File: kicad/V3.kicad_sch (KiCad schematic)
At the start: 3 parts, among them U1 SuperMini nRF52840

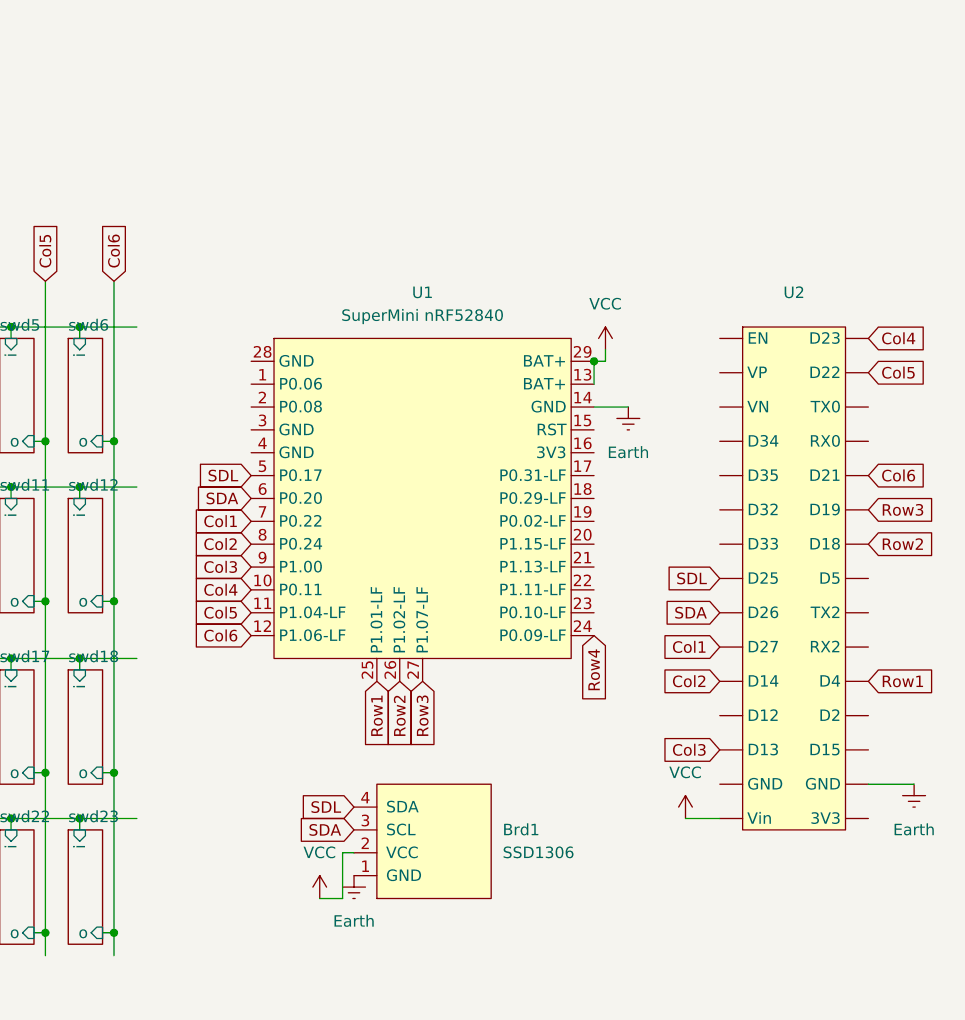
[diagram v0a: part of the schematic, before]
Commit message: change to esp32
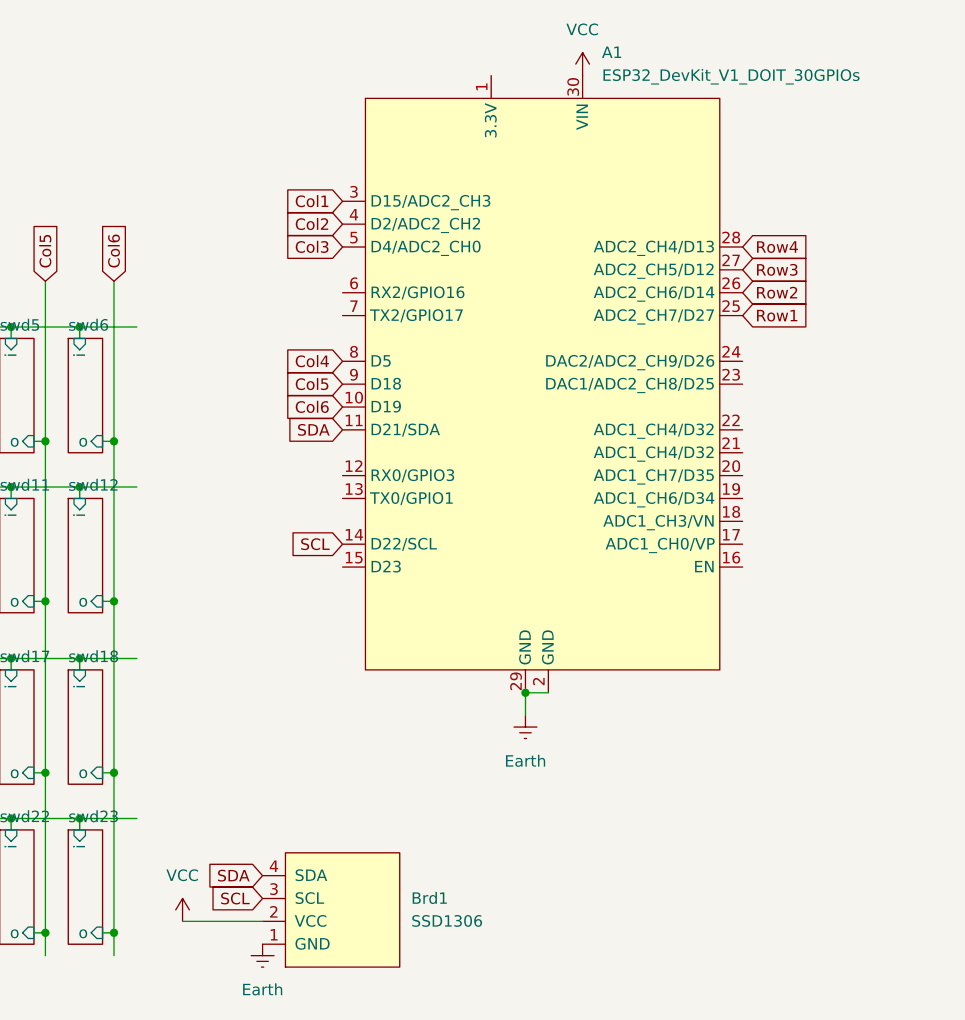
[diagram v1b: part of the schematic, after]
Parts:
- removed U1: SuperMini nRF52840, PCM_marbastlib-xp-promicroish:SuperMini_nRF52840_AH_USBup, symbol PCM_marbastlib-promicroish:SuperMini_nRF52840
- removed U2: ~, symbol Library:Esp32_Dev_Module
- added A1: ESP32_DevKit_V1_DOIT_30GPIOs, PCM_SL_Development_Boards:DOIT_ESP32_DEVKIT_30Pins, symbol PCM_SL_Development_Board:ESP32_DevKit_V1_DOIT_30GPIOs
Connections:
- net SDL is gone; now on net SDA: Brd1.4 (SDA)
- net Col1: now also A1.3 (D15/ADC2_CH3)
- net Col2: now also A1.4 (D2/ADC2_CH2)
- net Col3: now also A1.5 (D4/ADC2_CH0)
- net Col4: now also A1.8 (D5)
- net Col5: now also A1.9 (D18)
- net Col6: now also A1.10 (D19)
- net Earth: now also A1.2 (GND), A1.29 (GND)
- net Row1: now also A1.25 (ADC2_CH7/D27)
- net Row2: now also A1.26 (ADC2_CH6/D14)
- net Row3: now also A1.27 (ADC2_CH5/D12)
- net Row4: now also A1.28 (ADC2_CH4/D13)
- net SDA: now also A1.11 (D21/SDA); no longer Brd1.3 (SCL)
- net VCC: now also A1.30 (VIN)
- new net SCL: A1.14 (D22/SCL), Brd1.3 (SCL)
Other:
- moved on the sheet: Brd1

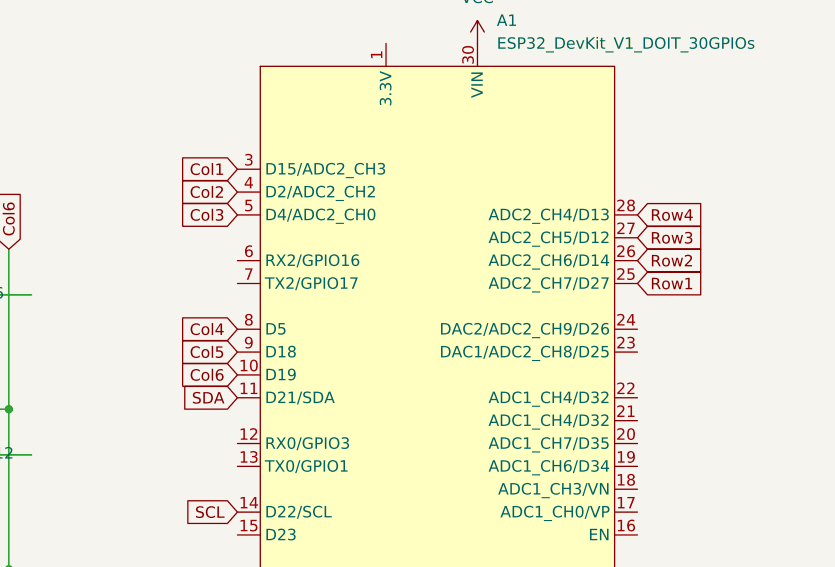
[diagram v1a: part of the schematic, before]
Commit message: problematic diodes
d2 and d34 cannot be used,d2 is the same pin as the builtin led, which
is used for serial confirmation rn, and d34 is input only
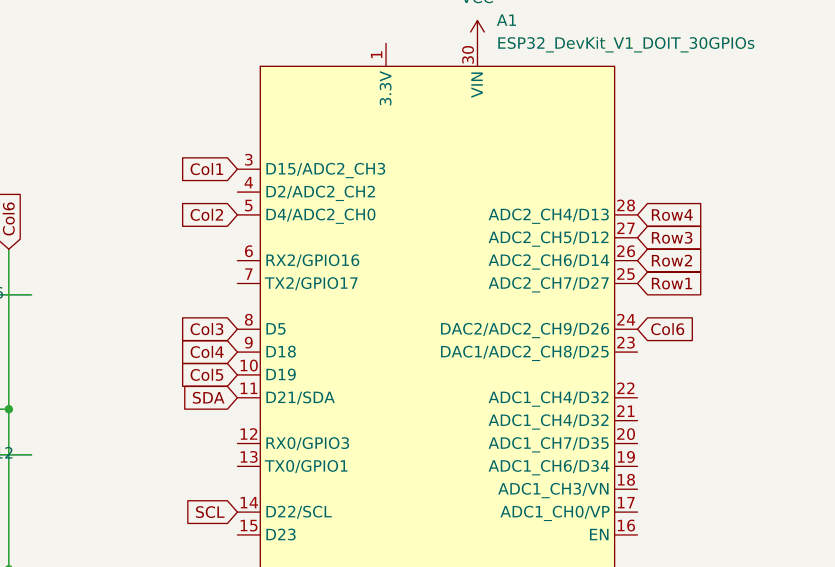
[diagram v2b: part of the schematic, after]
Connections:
- net Col2: now also A1.5 (D4/ADC2_CH0); no longer A1.4 (D2/ADC2_CH2)
- net Col3: now also A1.8 (D5); no longer A1.5 (D4/ADC2_CH0)
- net Col4: now also A1.9 (D18); no longer A1.8 (D5)
- net Col5: now also A1.10 (D19); no longer A1.9 (D18)
- net Col6: now also A1.24 (DAC2/ADC2_CH9/D26); no longer A1.10 (D19)
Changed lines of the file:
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@@
 	(global_label "Col3"
 		(shape input)
+		(at 143.51 63.5 180)
+		(fields_autoplaced yes)
+		(effects
+			(font
+				(size 1.27 1.27)
+			)
+			(justify right)
+		)
+		(property "Intersheetrefs" "${INTERSHEET_REFS}"
+			(at 136.2311 63.5 0)
+			(effects
+				(font
+					(size 1.27 1.27)
+				)
+				(justify right)
+				(hide yes)
+			)
+		)
+	)
+	(global_label "SCL"
+		(shape input)
+		(at 143.51 83.82 180)
+		(fields_autoplaced yes)
+		(effects
+			(font
+				(size 1.27 1.27)
+			)
+			(justify right)
+		)
+		(property "Intersheetrefs" "${INTERSHEET_REFS}"
+			(at 137.0172 83.82 0)
+			(effects
+				(font
+					(size 1.27 1.27)
+				)
+				(justify right)
+				(hide yes)
+			)
+		)
+	)
+	(global_label "Col4"
+		(shape input)
+		(at 143.51 66.04 180)
+		(fields_autoplaced yes)
+		(effects
+			(font
+				(size 1.27 1.27)
+			)
+			(justify right)
+		)
+		(property "Intersheetrefs" "${INTERSHEET_REFS}"
+			(at 136.2311 66.04 0)
+			(effects
+				(font
+					(size 1.27 1.27)
+				)
+				(justify right)
+				(hide yes)
+			)
+		)
+	)
+	(global_label "Col3"
+		(shape input)
+		(at 95.25 54.61 90)
+		(fields_autoplaced yes)
+		(effects
+			(font
+				(size 1.27 1.27)
+			)
+			(justify left)
+		)
+		(property "Intersheetrefs" "${INTERSHEET_REFS}"
+			(at 95.25 47.3311 90)
+			(effects
+				(font
+					(size 1.27 1.27)
+				)
+				(justify left)
+				(hide yes)
+			)
+		)
+	)
+	(global_label "Col6"
+		(shape input)
+		(at 187.96 63.5 0)
+		(fields_autoplaced yes)
+		(effects
+			(font
+				(size 1.27 1.27)
+			)
+			(justify left)
+		)
+		(property "Intersheetrefs" "${INTERSHEET_REFS}"
+			(at 195.2389 63.5 0)
+			(effects
+				(font
+					(size 1.27 1.27)
+				)
+				(justify left)
+				(hide yes)
+			)
+		)
+	)
+	(global_label "Col2"
+		(shape input)
+		(at 87.63 54.61 90)
+		(fields_autoplaced yes)
+		(effects
+			(font
+				(size 1.27 1.27)
+			)
+			(justify left)
+		)
+		(property "Intersheetrefs" "${INTERSHEET_REFS}"
+			(at 87.63 47.3311 90)
+			(effects
+				(font
+					(size 1.27 1.27)
+				)
+				(justify left)
+				(hide yes)
+			)
+		)
+	)
+	(global_label "Row3"
+		(shape input)
+		(at 187.96 53.34 0)
+		(fields_autoplaced yes)
+		(effects
+			(font
+				(size 1.27 1.27)
+			)
+			(justify left)
+		)
+		(property "Intersheetrefs" "${INTERSHEET_REFS}"
+			(at 195.9042 53.34 0)
+			(effects
+				(font
+					(size 1.27 1.27)
+				)
+				(justify left)
+				(hide yes)
+			)
+		)
+	)
+	(global_label "Col2"
+		(shape input)
 		(at 143.51 50.8 180)
 		(fields_autoplaced yes)
@@
 		)
 	)
-	(global_label "SCL"
-		(shape input)
-		(at 143.51 83.82 180)
-		(fields_autoplaced yes)
-		(effects
-			(font
-				(size 1.27 1.27)
-			)
-			(justify right)
-		)
-		(property "Intersheetrefs" "${INTERSHEET_REFS}"
-			(at 137.0172 83.82 0)
-			(effects
-				(font
-					(size 1.27 1.27)
-				)
-				(justify right)
-				(hide yes)
-			)
-		)
-	)
-	(global_label "Col4"
-		(shape input)
-		(at 143.51 63.5 180)
-		(fields_autoplaced yes)
-		(effects
-			(font
-				(size 1.27 1.27)
-			)
-			(justify right)
-		)
-		(property "Intersheetrefs" "${INTERSHEET_REFS}"
-			(at 136.2311 63.5 0)
-			(effects
-				(font
-					(size 1.27 1.27)
-				)
-				(justify right)
-				(hide yes)
-			)
-		)
-	)
-	(global_label "Col3"
-		(shape input)
-		(at 95.25 54.61 90)
-		(fields_autoplaced yes)
-		(effects
-			(font
-				(size 1.27 1.27)
-			)
-			(justify left)
-		)
-		(property "Intersheetrefs" "${INTERSHEET_REFS}"
-			(at 95.25 47.3311 90)
-			(effects
-				(font
-					(size 1.27 1.27)
-				)
-				(justify left)
-				(hide yes)
-			)
-		)
-	)
 	(global_label "Col6"
 		(shape input)
+		(at 118.11 54.61 90)
+		(fields_autoplaced yes)
+		(effects
+			(font
+				(size 1.27 1.27)
+			)
+			(justify left)
+		)
+		(property "Intersheetrefs" "${INTERSHEET_REFS}"
+			(at 118.11 47.3311 90)
+			(effects
+				(font
+					(size 1.27 1.27)
+				)
+				(justify left)
+				(hide yes)
+			)
+		)
+	)
+	(global_label "Row1"
+		(shape input)
+		(at 71.12 59.69 180)
+		(fields_autoplaced yes)
+		(effects
+			(font
+				(size 1.27 1.27)
+			)
+			(justify right)
+		)
+		(property "Intersheetrefs" "${INTERSHEET_REFS}"
+			(at 63.1758 59.69 0)
+			(effects
+				(font
+					(size 1.27 1.27)
+				)
+				(justify right)
+				(hide yes)
+			)
+		)
+	)
+	(global_label "Col5"
+		(shape input)
 		(at 143.51 68.58 180)
 		(fields_autoplaced yes)
@@
 			(effects
 				(font
-					(size 1.27 1.27)
-				)
-				(justify right)
-				(hide yes)
-			)
-		)
-	)
-	(global_label "Col2"
-		(shape input)
-		(at 87.63 54.61 90)
-		(fields_autoplaced yes)
-		(effects
-			(font
-				(size 1.27 1.27)
-			)
-			(justify left)
-		)
-		(property "Intersheetrefs" "${INTERSHEET_REFS}"
-			(at 87.63 47.3311 90)
-			(effects
-				(font
-					(size 1.27 1.27)
-				)
-				(justify left)
-				(hide yes)
-			)
-		)
-	)
-	(global_label "Row3"
-		(shape input)
-		(at 187.96 53.34 0)
-		(fields_autoplaced yes)
-		(effects
-			(font
-				(size 1.27 1.27)
-			)
-			(justify left)
-		)
-		(property "Intersheetrefs" "${INTERSHEET_REFS}"
-			(at 195.9042 53.34 0)
-			(effects
-				(font
-					(size 1.27 1.27)
-				)
-				(justify left)
-				(hide yes)
-			)
-		)
-	)
-	(global_label "Col2"
-		(shape input)
-		(at 143.51 48.26 180)
-		(fields_autoplaced yes)
-		(effects
-			(font
-				(size 1.27 1.27)
-			)
-			(justify right)
-		)
-		(property "Intersheetrefs" "${INTERSHEET_REFS}"
-			(at 136.2311 48.26 0)
-			(effects
-				(font
-					(size 1.27 1.27)
-				)
-				(justify right)
-				(hide yes)
-			)
-		)
-	)
-	(global_label "Col6"
-		(shape input)
-		(at 118.11 54.61 90)
-		(fields_autoplaced yes)
-		(effects
-			(font
-				(size 1.27 1.27)
-			)
-			(justify left)
-		)
-		(property "Intersheetrefs" "${INTERSHEET_REFS}"
-			(at 118.11 47.3311 90)
-			(effects
-				(font
-					(size 1.27 1.27)
-				)
-				(justify left)
-				(hide yes)
-			)
-		)
-	)
-	(global_label "Row1"
-		(shape input)
-		(at 71.12 59.69 180)
-		(fields_autoplaced yes)
-		(effects
-			(font
-				(size 1.27 1.27)
-			)
-			(justify right)
-		)
-		(property "Intersheetrefs" "${INTERSHEET_REFS}"
-			(at 63.1758 59.69 0)
-			(effects
-				(font
-					(size 1.27 1.27)
-				)
-				(justify right)
-				(hide yes)
-			)
-		)
-	)
-	(global_label "Col5"
-		(shape input)
-		(at 143.51 66.04 180)
-		(fields_autoplaced yes)
-		(effects
-			(font
-				(size 1.27 1.27)
-			)
-			(justify right)
-		)
-		(property "Intersheetrefs" "${INTERSHEET_REFS}"
-			(at 136.2311 66.04 0)
-			(effects
-				(font

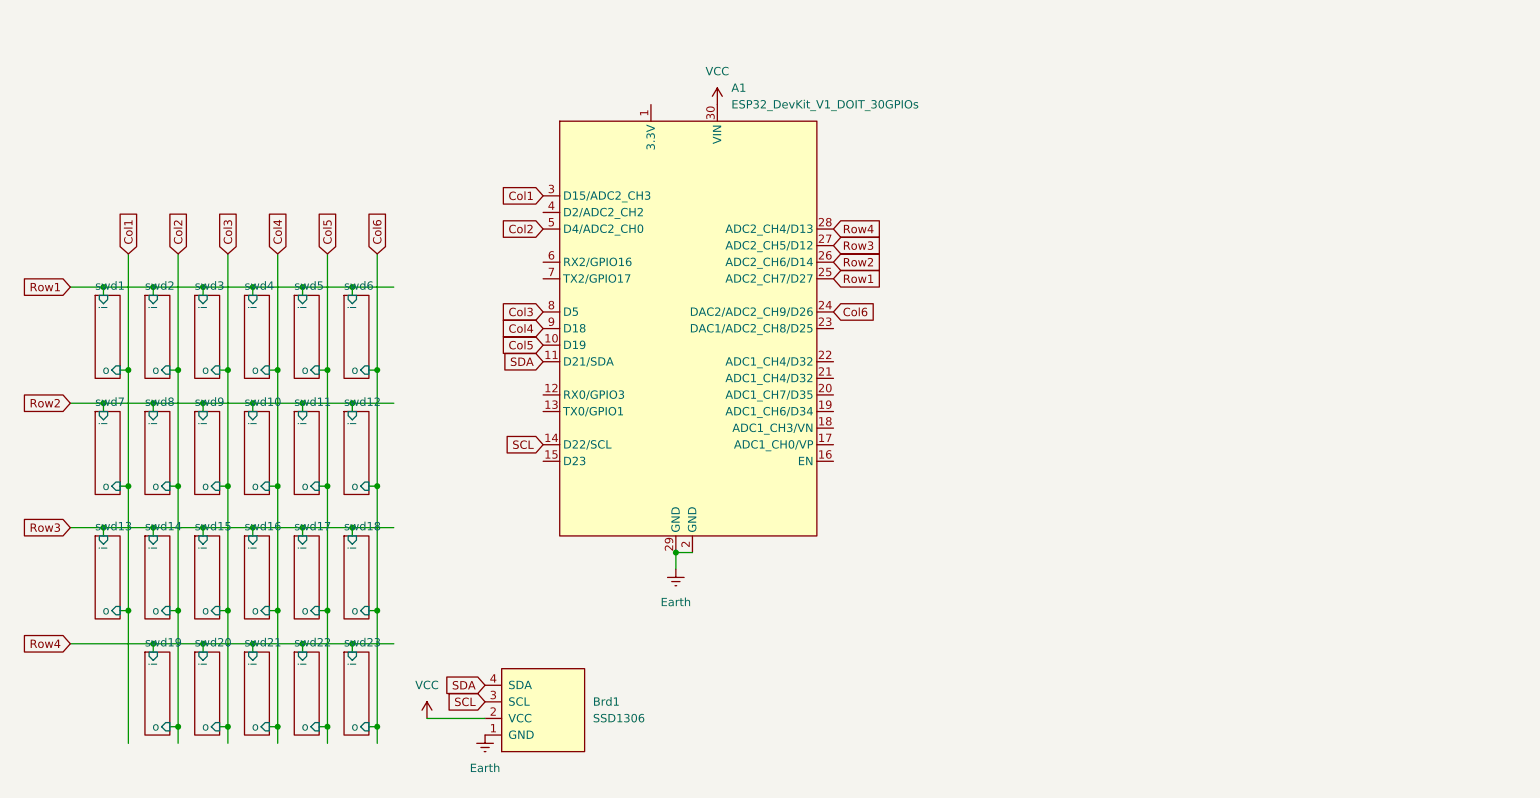
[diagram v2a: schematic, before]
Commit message: change from global to sheet labels
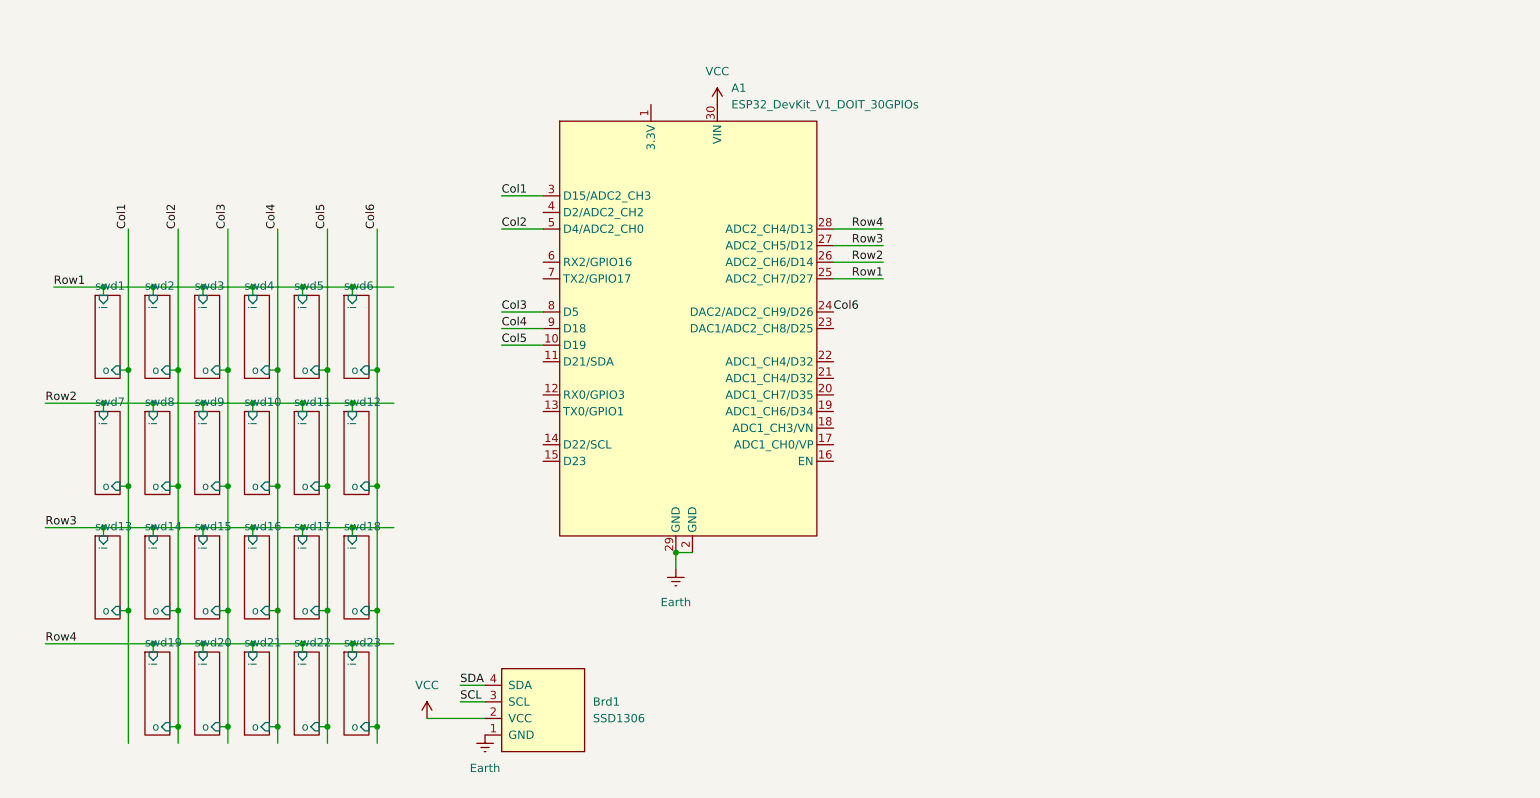
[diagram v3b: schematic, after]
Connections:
- net SCL: no longer A1.14 (D22/SCL)
- net SDA: no longer A1.11 (D21/SDA)

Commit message: battery chargin module additon
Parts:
- added BT1: Battery_Cell, symbol Device:Battery_Cell
- added U1: ~, Library:HAYATEC TP4056 LIPO CHARGING MODULE, symbol Library:TP4056_usb_module
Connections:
- net Earth: now also U1.2 (Gin), U1.5 (Out-)
- net SCL: now also A1.14 (D22/SCL)
- net SDA: now also A1.11 (D21/SDA)
- net VCC: now also U1.4 (Vin)
- net -3V3: now reaches A1.1 (3.3V)
- net -3V3: now also U1.1 (Out+)
- new net: BT1.1 (+), U1.3 (B+)
- new net: BT1.2 (-), U1.6 (B-)
- no-connect marks 0 -> 1

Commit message: usp+uart converter
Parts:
- added U2: ~, Library:CH340C_pins, symbol Library:CH340C_usb_module
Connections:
- net -3V3: now also U2.1 (3v3)
- net Earth: now also U2.6 (GND)
- net RX: now reaches A1.12 (RX0/GPIO3)
- net RX: now also U2.3 (RXD)
- net TX: now reaches A1.13 (TX0/GPIO1)
- net TX: now also U2.4 (TXD)
